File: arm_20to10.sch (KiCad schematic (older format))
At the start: 14 parts, among them J1 SFH11-PBPC-D10-RA-BK, J2 CONN_02X10, J3 CONN_02X05, J4 CONN_02X05, J5 CONN_02X05, J6 MF-CON-2.54mm-2x3, SW1 OS102011MA1QS1, U1 MIC5504-3.3YM5 TR

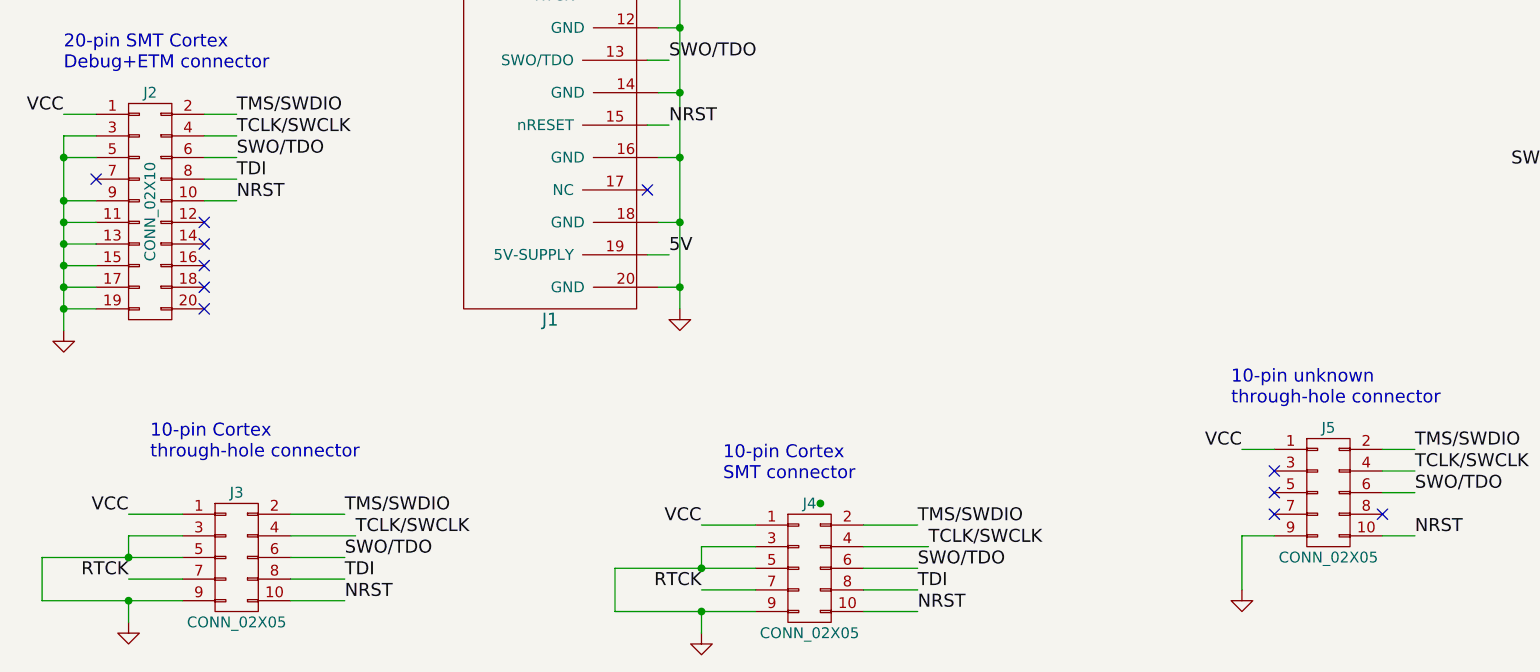
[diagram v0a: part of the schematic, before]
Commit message: update project to look in my library for my custom parts rather than Noah's
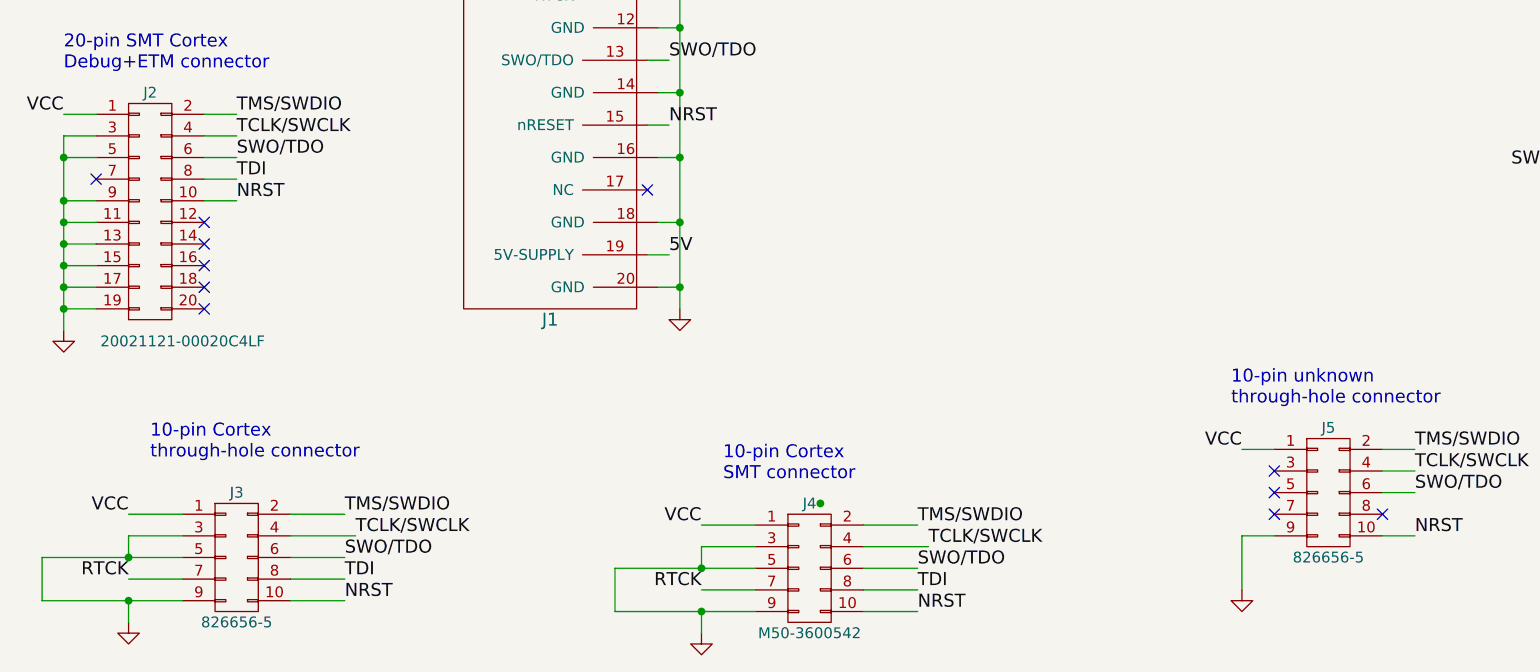
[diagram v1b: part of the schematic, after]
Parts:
- D1, D2: footprint kicadlib:SMD_0603_LED -> kes_custom:SMD_0603_LED
- J2: value CONN_02X10 -> 20021121-00020C4LF; footprint kicadlib:ARM_20_PIN_SMT -> kes_custom:ARM_20_PIN_SMT
- J3, J5: value CONN_02X05 -> 826656-5
- J4: value CONN_02X05 -> M50-3600542
- SW1: footprint kicadlib:SS-12D07-VG-kes -> kes_custom:slideswitch-OS102011MA1QS1
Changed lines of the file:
@@
 F 0 "SW1" H 8950 1850 50  0000 C CNN
 F 1 "OS102011MA1QS1" H 9000 1550 50  0000 C CNN
-F 2 "kicadlib:SS-12D07-VG-kes" H 9150 1700 60  0001 C CNN
+F 2 "kes_custom:slideswitch-OS102011MA1QS1" H 9150 1700 60  0001 C CNN
 F 3 "~" H 9150 1700 60  0000 C CNN
 F 4 "C&K" H 9150 1700 60  0001 C CNN "MFG Name"
@@
 F 0 "D2" H 9450 1200 50  0000 C CNN
 F 1 "LED" H 9450 1000 50  0000 C CNN
-F 2 "kicadlib:SMD_0603_LED" H 9450 1100 60  0001 C CNN
+F 2 "kes_custom:SMD_0603_LED" H 9450 1100 60  0001 C CNN
 F 3 "~" H 9450 1100 60  0000 C CNN
 	1    9450 1100
@@
 F 0 "D1" H 6600 2000 50  0000 C CNN
 F 1 "LED" H 6600 1800 50  0000 C CNN
-F 2 "kicadlib:SMD_0603_LED" H 6600 1900 60  0001 C CNN
+F 2 "kes_custom:SMD_0603_LED" H 6600 1900 60  0001 C CNN
 F 3 "~" H 6600 1900 60  0000 C CNN
 	1    6600 1900
@@
 P 1950 6350
 F 0 "J3" H 1950 6650 50  0000 C CNN
-F 1 "CONN_02X05" H 1950 6050 50  0000 C CNN
+F 1 "826656-5" H 1950 6050 50  0000 C CNN
 F 2 "Pin_Headers:Pin_Header_Straight_2x05" H 1950 5150 50  0001 C CNN
 F 3 "" H 1950 5150 50  0000 C CNN
@@
 P 4600 6400
 F 0 "J4" H 4600 6700 50  0000 C CNN
-F 1 "CONN_02X05" H 4600 6100 50  0000 C CNN
+F 1 "M50-3600542" H 4600 6100 50  0000 C CNN
 F 2 "kicadlib:ARM_10_PIN_SMT" H 4600 5200 50  0001 C CNN
 F 3 "" H 4600 5200 50  0000 C CNN
@@
 P 1550 4750
 F 0 "J2" H 1550 5300 50  0000 C CNN
-F 1 "CONN_02X10" V 1550 4750 50  0000 C CNN
-F 2 "kicadlib:ARM_20_PIN_SMT" H 1550 3550 50  0001 C CNN
+F 1 "20021121-00020C4LF" H 1700 4150 50  0000 C CNN
+F 2 "kes_custom:ARM_20_PIN_SMT" H 1550 3550 50  0001 C CNN
 F 3 "" H 1550 3550 50  0000 C CNN
 	1    1550 4750
@@
 P 7000 6050
 F 0 "J5" H 7000 6350 50  0000 C CNN
-F 1 "CONN_02X05" H 7000 5750 50  0000 C CNN
+F 1 "826656-5" H 7000 5750 50  0000 C CNN
 F 2 "Pin_Headers:Pin_Header_Straight_2x05" H 7000 4850 50  0001 C CNN
 F 3 "" H 7000 4850 50  0000 C CNN
